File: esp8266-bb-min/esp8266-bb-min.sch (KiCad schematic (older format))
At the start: 24 parts, among them J1 Conn_01x02_Male, J2 Conn_01x04_Male, J3 Conn_01x04_Male, J4 Conn_01x06_Male, J5 Conn_01x04_Male, J6 Conn_01x04_Male, J7 Conn_01x02_Male, U1 LP38693MP-3.3, U2 ESP-12F

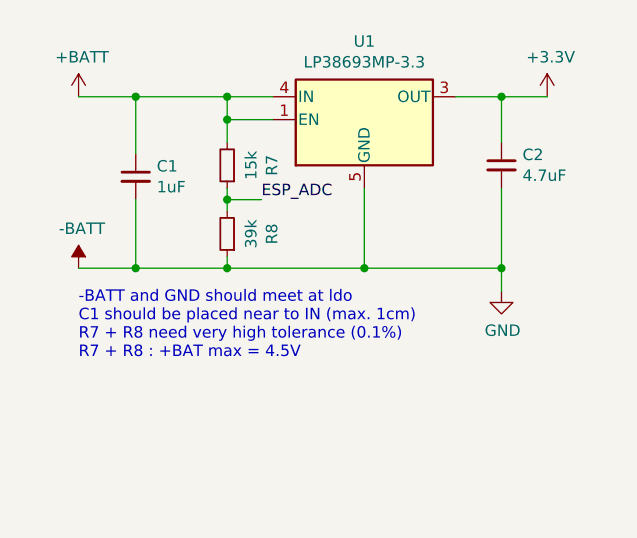
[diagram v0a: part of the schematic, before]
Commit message: sch: corrected resistor values for ADC
Signed-off-by: Dominik Laton <dominik.laton@web.de>
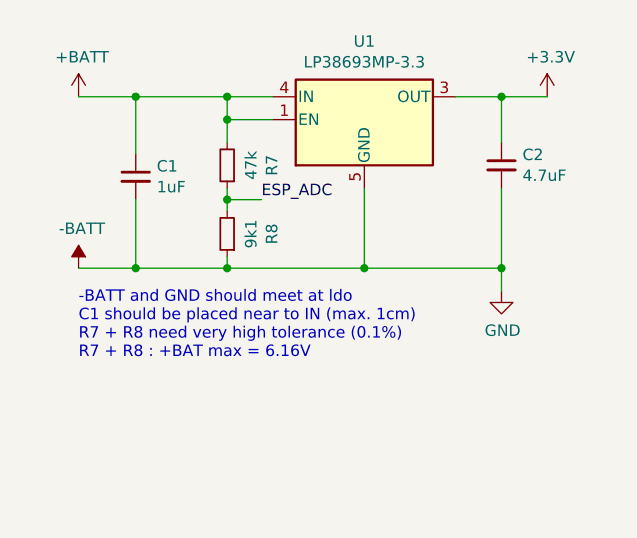
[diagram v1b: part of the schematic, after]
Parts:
- R7: value 15k -> 47k
- R8: value 39k -> 9k1
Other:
- note added: "-BATT and GND should meet at ldo\nC1 should be placed near to IN (max. 1cm)\nR7 + R8 need very high tolerance (0.1%)\nR7 + R8 : +BAT max = 6.16V"
- note removed: "-BATT and GND should meet at ldo\nC1 should be placed near to IN (max. 1cm)\nR7 + R8 need very high tolerance (0.1%)\nR7 + R8 : +BAT max = 4.5V"
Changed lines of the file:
@@
 P 3400 1700
 F 0 "R7" V 3204 1700 50  0000 C CNN
-F 1 "15k" V 3295 1700 50  0000 C CNN
+F 1 "47k" V 3295 1700 50  0000 C CNN
 F 2 "Resistor_SMD:R_0805_2012Metric_Pad1.20x1.40mm_HandSolder" H 3400 1700 50  0001 C CNN
 F 3 "~" H 3400 1700 50  0001 C CNN
@@
 	9600 3400 9800 3400
 Text Notes 2750 2550 0    50   ~ 0
--BATT and GND should meet at ldo\nC1 should be placed near to IN (max. 1cm)\nR7 + R8 need very high tolerance (0.1%)\nR7 + R8 : +BAT max = 4.5V
+-BATT and GND should meet at ldo\nC1 should be placed near to IN (max. 1cm)\nR7 + R8 need very high tolerance (0.1%)\nR7 + R8 : +BAT max = 6.16V
 $Comp
 L Connector:Conn_01x04_Male J2
@@
 P 3400 2000
 F 0 "R8" V 3204 2000 50  0000 C CNN
-F 1 "39k" V 3295 2000 50  0000 C CNN
+F 1 "9k1" V 3295 2000 50  0000 C CNN
 F 2 "Resistor_SMD:R_0805_2012Metric_Pad1.20x1.40mm_HandSolder" H 3400 2000 50  0001 C CNN
 F 3 "~" H 3400 2000 50  0001 C CNN
